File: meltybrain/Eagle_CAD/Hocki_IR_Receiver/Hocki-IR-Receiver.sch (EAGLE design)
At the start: 70 parts, among them J1 SM03B-SRSS-TB(LF)(SN), U1 OPA2380AIDGKR, U10 NL27WZ32USG, U11 TMUX1204DGSR, U2 OPA2380AIDGKR, U3 AP2210K-5.0TRG1, U4 LMH6612MAX/NOPB, U5 LMH6612MAX/NOPB, U6 TLV73310PDBVT, U7 TLV3502AIDCNR, U8 TLV3502AIDCNR, U9 SN74LVC1G58DCKR

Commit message: schematic updates
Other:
- moved on the sheet: C14, C16, R15, R26

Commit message: IR Receiver schematic edits. Added ldo protection
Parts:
- added D10, D11: BAS581-02V-V-G-08, Hocki_Library:BAS581-02V-V-G-08
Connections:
- net N$15 renamed 10KPEAK_BUF
- net N$16 renamed 1MPEAK_BUF
- net N$17 renamed 1MPEAK
- net N$18 renamed 100KPEAK_BUF
- net 1.0V: now also D11.A
- net 5V: now also D10.A, D11.C
- net 9V: now also D10.C
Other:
- note added: "Comparator W/ Hyst"
- note added: "Multiplexer And Connector"
- note added: "Multiplexer Logic: A1=A+B A0=A+!B!C"
- note added: "Peak Buffering"
- note added: "Peak Detector"
- note added: "Power Regulation"
- note added: "Transimpedance"
- note removed: "Logic: A1=A+B A0=A+!B!C"
- moved on the sheet: C1, C10, C11, C12, C13, C14, C15, C16, C17, C2, C3, C4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

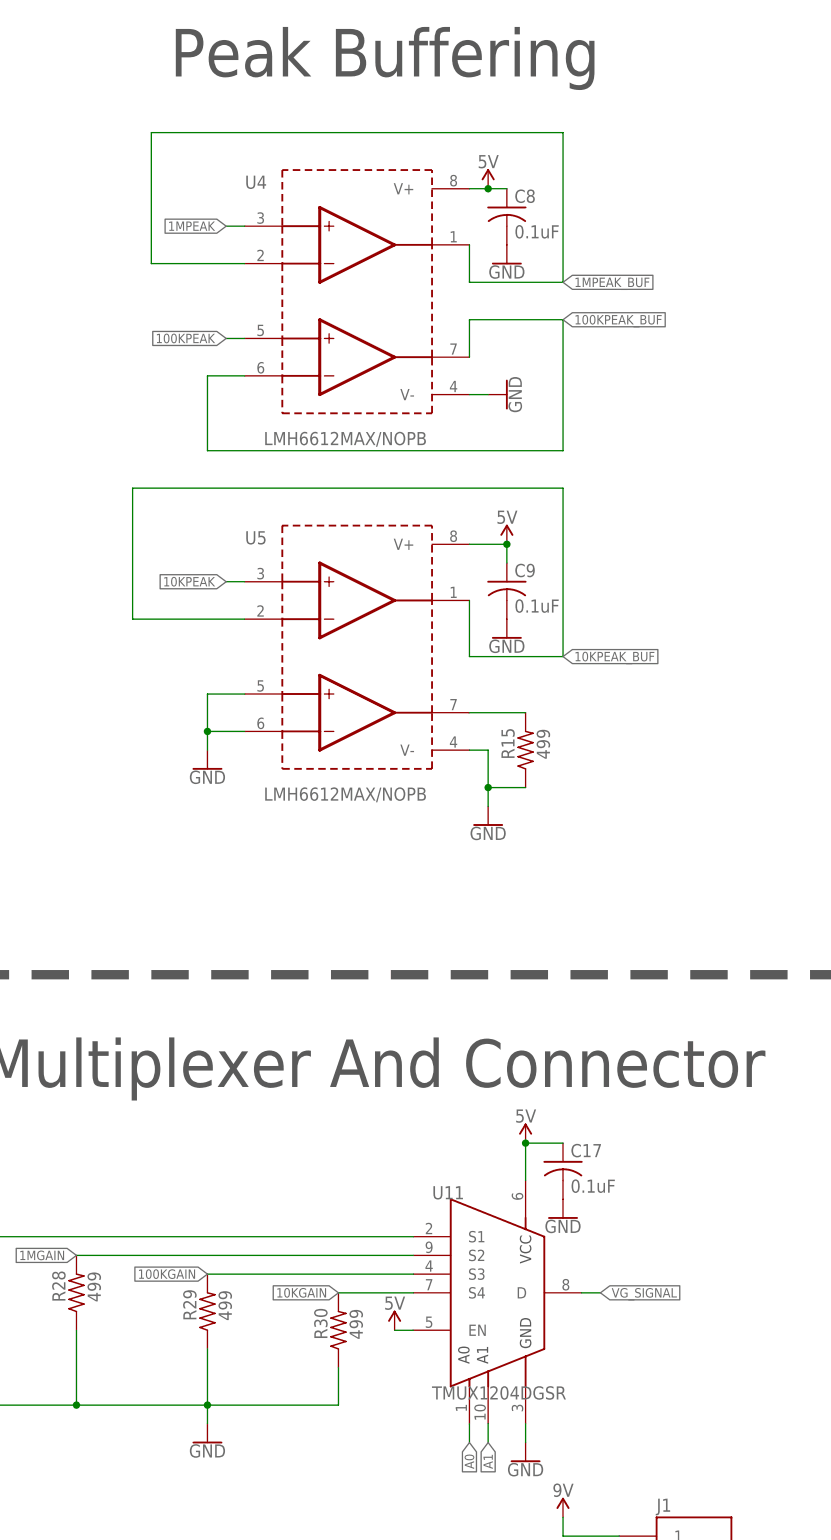
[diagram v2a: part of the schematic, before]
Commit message: Edited silkscreen and made minor changes to IR Receiver silkscreen and schematic
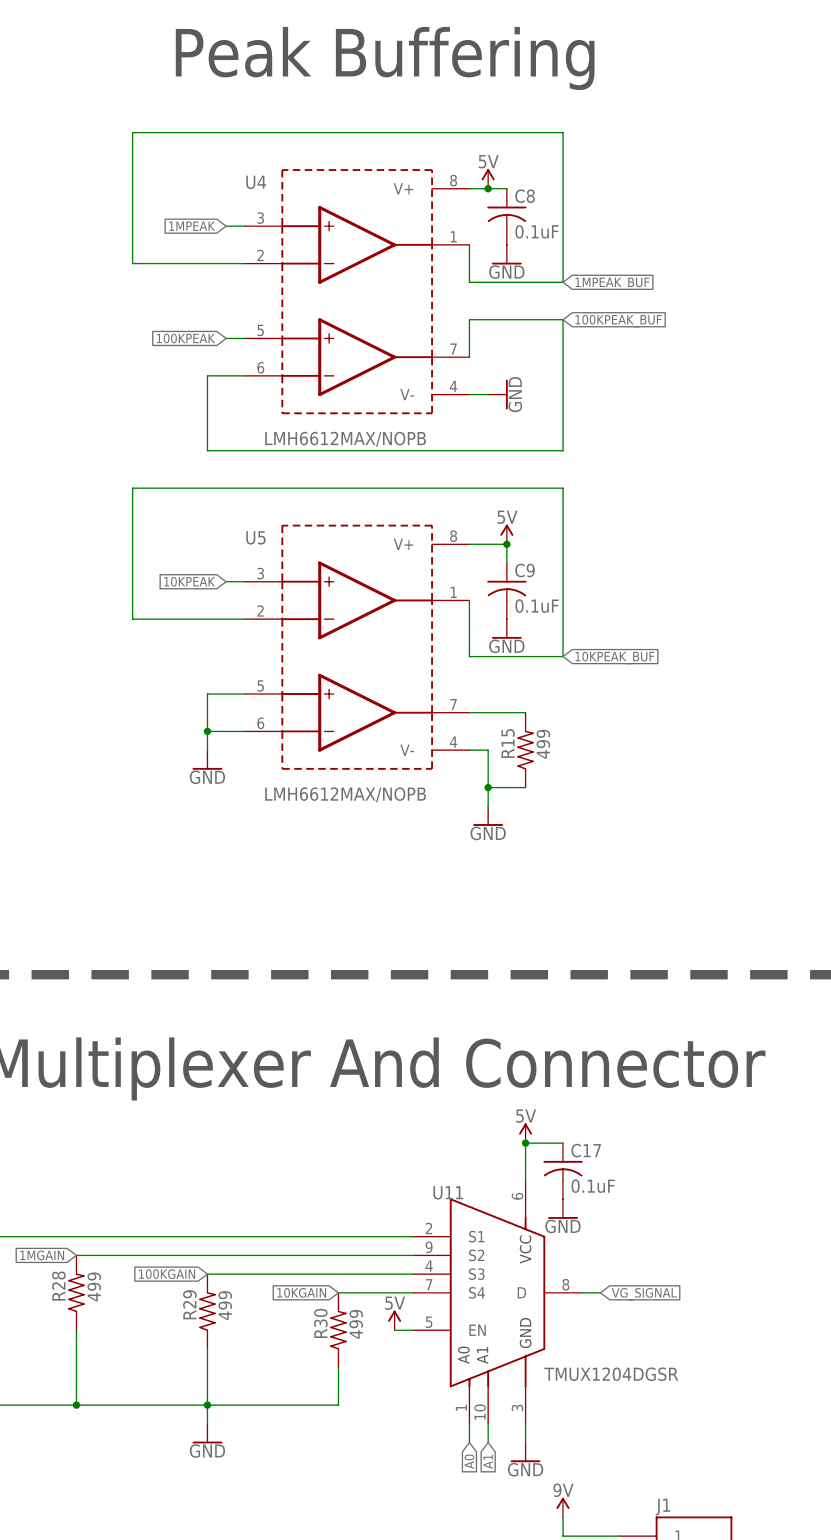
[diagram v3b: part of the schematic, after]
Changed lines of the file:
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@@
 <instance part="U11" gate="A" x="157.48" y="-43.18" smashed="yes">
 <attribute name="NAME" x="147.32" y="-30.48" size="1.778" layer="95"/>
-<attribute name="VALUE" x="147.32" y="-55.88" size="1.778" layer="96" align="top-left"/>
+<attribute name="VALUE" x="162.56" y="-53.34" size="1.778" layer="96" align="top-left"/>
 </instance>
 <instance part="R20" gate="G$1" x="-172.72" y="-25.4" smashed="yes" rot="R90">
@@
 <pinref part="U4" gate="A" pin="OUTA"/>
 <pinref part="U4" gate="A" pin="INA-"/>
-<wire x1="121.92" y1="96.52" x2="109.22" y2="96.52" width="0.1524" layer="91"/>
-<wire x1="109.22" y1="96.52" x2="109.22" y2="114.3" width="0.1524" layer="91"/>
-<wire x1="109.22" y1="114.3" x2="165.1" y2="114.3" width="0.1524" layer="91"/>
+<wire x1="121.92" y1="96.52" x2="106.68" y2="96.52" width="0.1524" layer="91"/>
+<wire x1="106.68" y1="96.52" x2="106.68" y2="114.3" width="0.1524" layer="91"/>
+<wire x1="106.68" y1="114.3" x2="165.1" y2="114.3" width="0.1524" layer="91"/>
 <wire x1="165.1" y1="93.98" x2="165.1" y2="114.3" width="0.1524" layer="91"/>
 <wire x1="152.4" y1="99.06" x2="152.4" y2="93.98" width="0.1524" layer="91"/>

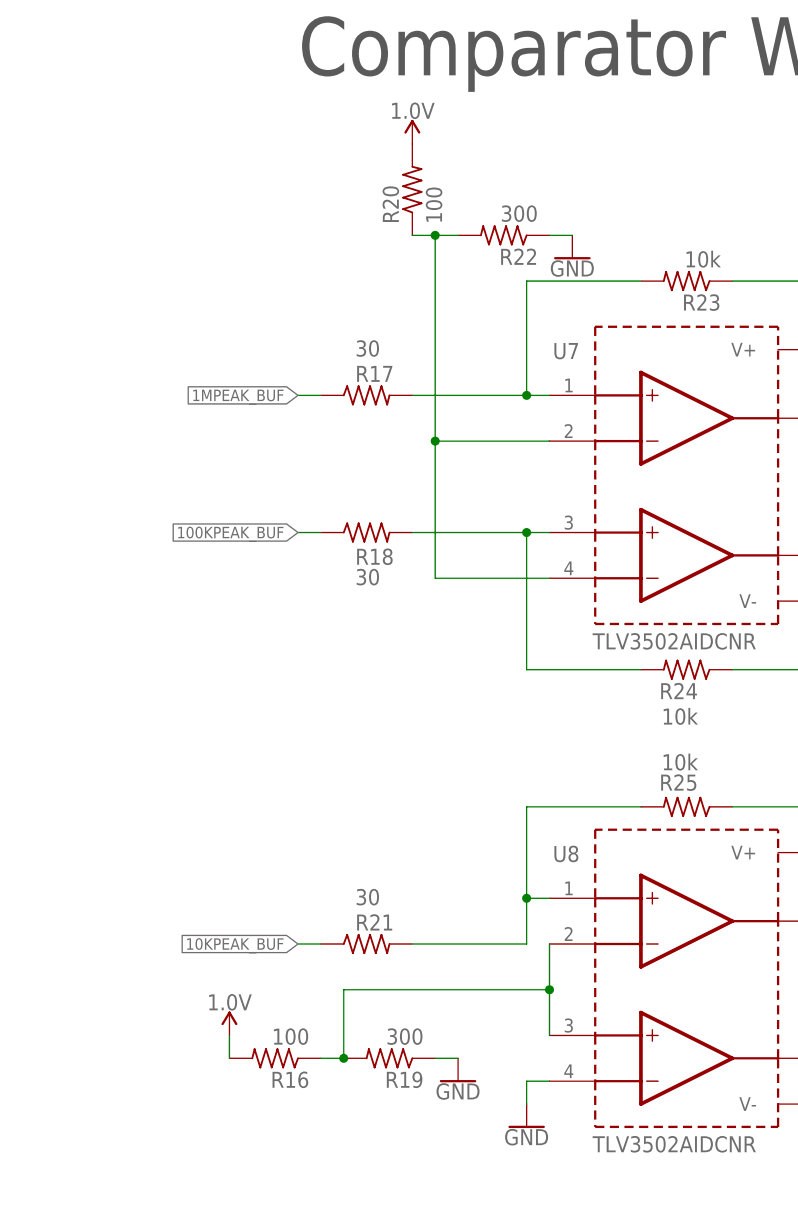
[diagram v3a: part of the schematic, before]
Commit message: comparator trigger point fixed
assumed diode voltage drop was constant originally
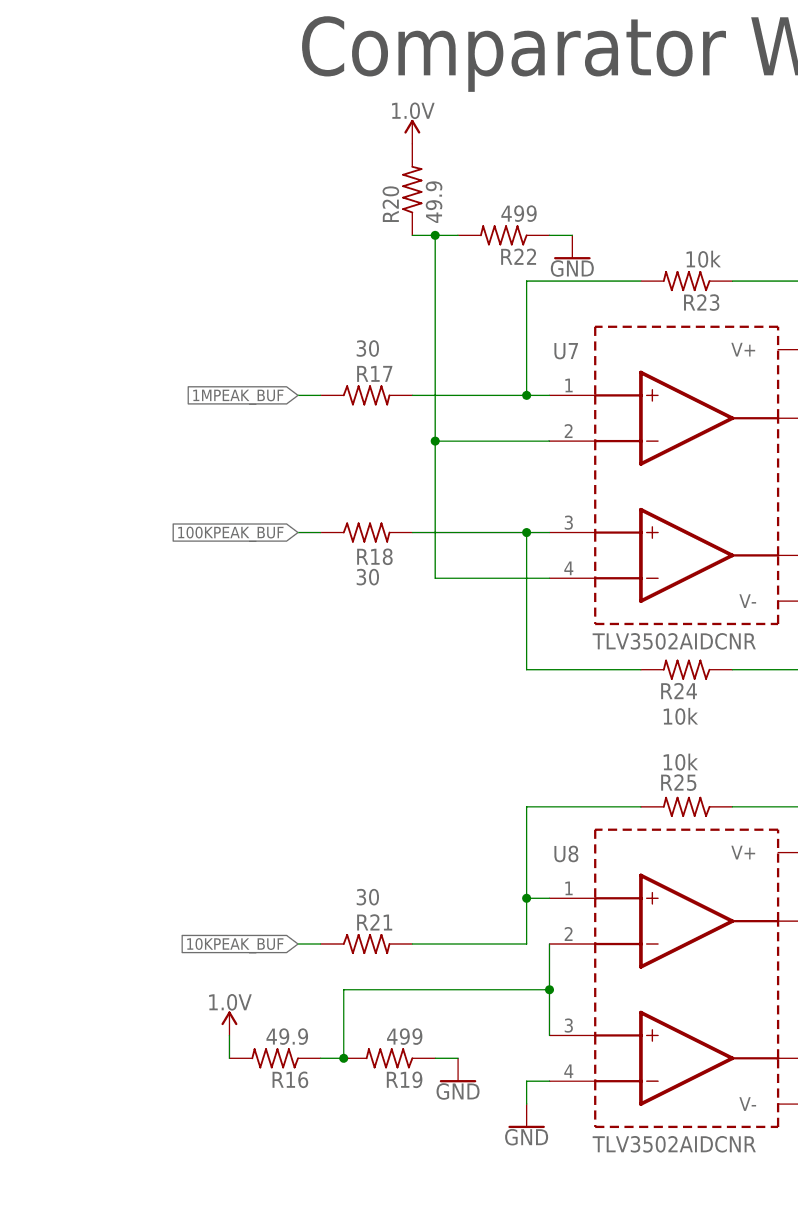
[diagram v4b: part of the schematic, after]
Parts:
- R16, R20: value 100 -> 49.9
- R19, R22: value 300 -> 499
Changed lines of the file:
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@@
 <part name="SUPPLY10" library="SparkFun-PowerSymbols" deviceset="5V" device=""/>
 <part name="U11" library="Hocki_Library" deviceset="TMUX1204DGSR" device=""/>
-<part name="R20" library="resistor" library_urn="urn:adsk.eagle:library:348" deviceset="R-US_" device="R0603" package3d_urn="urn:adsk.eagle:package:26057/1" value="100"/>
-<part name="R22" library="resistor" library_urn="urn:adsk.eagle:library:348" deviceset="R-US_" device="R0603" package3d_urn="urn:adsk.eagle:package:26057/1" value="300"/>
+<part name="R20" library="resistor" library_urn="urn:adsk.eagle:library:348" deviceset="R-US_" device="R0603" package3d_urn="urn:adsk.eagle:package:26057/1" value="49.9"/>
+<part name="R22" library="resistor" library_urn="urn:adsk.eagle:library:348" deviceset="R-US_" device="R0603" package3d_urn="urn:adsk.eagle:package:26057/1" value="499"/>
 <part name="GND14" library="SparkFun-PowerSymbols" deviceset="GND" device=""/>
-<part name="R16" library="resistor" library_urn="urn:adsk.eagle:library:348" deviceset="R-US_" device="R0603" package3d_urn="urn:adsk.eagle:package:26057/1" value="100"/>
-<part name="R19" library="resistor" library_urn="urn:adsk.eagle:library:348" deviceset="R-US_" device="R0603" package3d_urn="urn:adsk.eagle:package:26057/1" value="300"/>
+<part name="R16" library="resistor" library_urn="urn:adsk.eagle:library:348" deviceset="R-US_" device="R0603" package3d_urn="urn:adsk.eagle:package:26057/1" value="49.9"/>
+<part name="R19" library="resistor" library_urn="urn:adsk.eagle:library:348" deviceset="R-US_" device="R0603" package3d_urn="urn:adsk.eagle:package:26057/1" value="499"/>
 <part name="SUPPLY11" library="SparkFun-PowerSymbols" deviceset="5V" device=""/>
 <part name="GND15" library="SparkFun-PowerSymbols" deviceset="GND" device=""/>

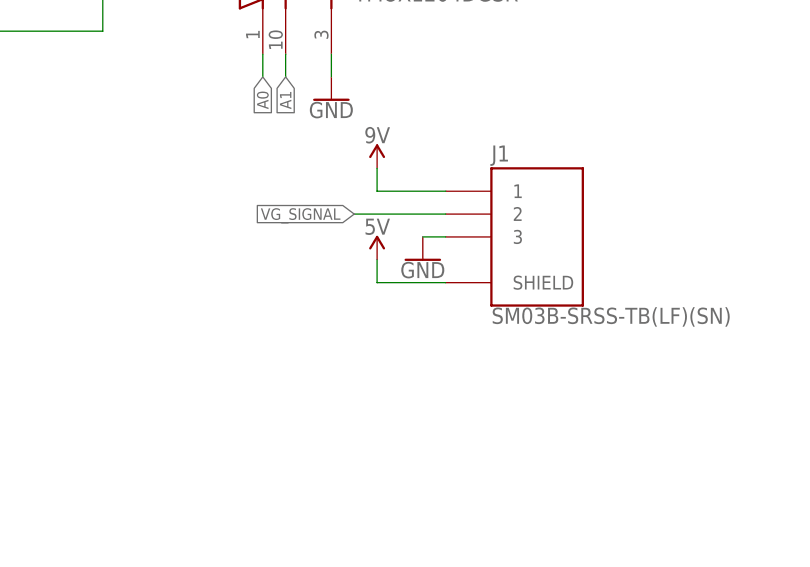
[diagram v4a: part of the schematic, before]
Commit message: receiver now 4 layers
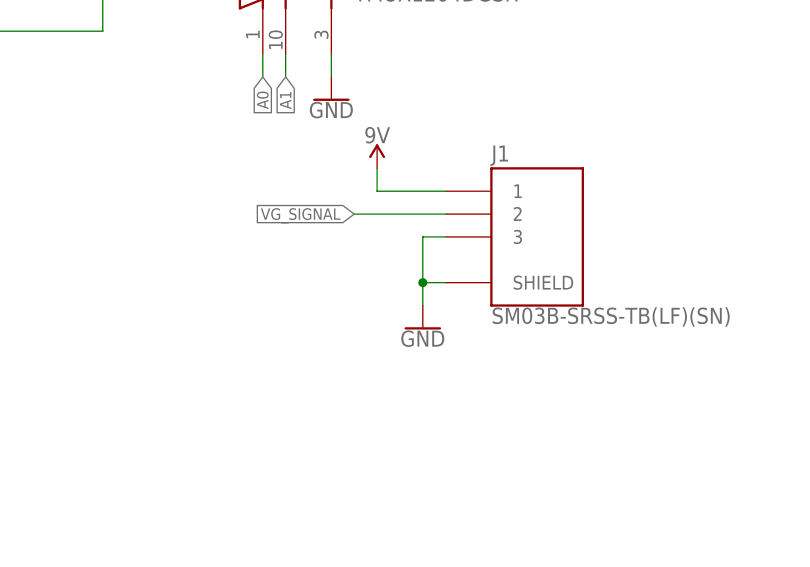
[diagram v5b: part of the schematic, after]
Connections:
- net 5V: no longer J1.SHIELD
- net GND: now also J1.SHIELD
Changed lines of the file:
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@@
 <part name="SUPPLY17" library="Hocki_Library" deviceset="9V" device=""/>
 <part name="GND34" library="SparkFun-PowerSymbols" deviceset="GND" device=""/>
-<part name="SUPPLY18" library="SparkFun-PowerSymbols" deviceset="5V" device=""/>
 <part name="J1" library="Hocki_Library" deviceset="SM03B-SRSS-TB(LF)(SN)" device="" package3d_urn="urn:adsk.eagle:package:22261818/2"/>
 <part name="D8" library="SparkFun-LED" deviceset="LED-GREEN" device="0603" value="GREEN"/>
@@
 <attribute name="VALUE" x="165.1" y="-70.866" size="1.778" layer="96" align="bottom-center"/>
 </instance>
-<instance part="GND34" gate="1" x="170.18" y="-83.82" smashed="yes">
-<attribute name="VALUE" x="170.18" y="-84.074" size="1.778" layer="96" align="top-center"/>
-</instance>
-<instance part="SUPPLY18" gate="G$1" x="165.1" y="-83.82" smashed="yes">
-<attribute name="VALUE" x="165.1" y="-81.026" size="1.778" layer="96" align="bottom-center"/>
+<instance part="GND34" gate="1" x="170.18" y="-91.44" smashed="yes">
+<attribute name="VALUE" x="170.18" y="-91.694" size="1.778" layer="96" align="top-center"/>
 </instance>
 <instance part="J1" gate="G$1" x="182.88" y="-81.28" smashed="yes">
@@
 <pinref part="J1" gate="G$1" pin="3"/>
 <wire x1="172.72" y1="-81.28" x2="170.18" y2="-81.28" width="0.1524" layer="91"/>
+<wire x1="170.18" y1="-81.28" x2="170.18" y2="-86.36" width="0.1524" layer="91"/>
+<pinref part="J1" gate="G$1" pin="SHIELD"/>
+<wire x1="170.18" y1="-86.36" x2="170.18" y2="-88.9" width="0.1524" layer="91"/>
+<wire x1="172.72" y1="-86.36" x2="170.18" y2="-86.36" width="0.1524" layer="91"/>
+<junction x="170.18" y="-86.36"/>
 </segment>
 <segment>
@@
 </segment>
 <segment>
-<wire x1="172.72" y1="-86.36" x2="165.1" y2="-86.36" width="0.1524" layer="91"/>
-<pinref part="SUPPLY18" gate="G$1" pin="5V"/>
-<wire x1="165.1" y1="-86.36" x2="165.1" y2="-83.82" width="0.1524" layer="91"/>
-<pinref part="J1" gate="G$1" pin="SHIELD"/>
-</segment>
-<segment>

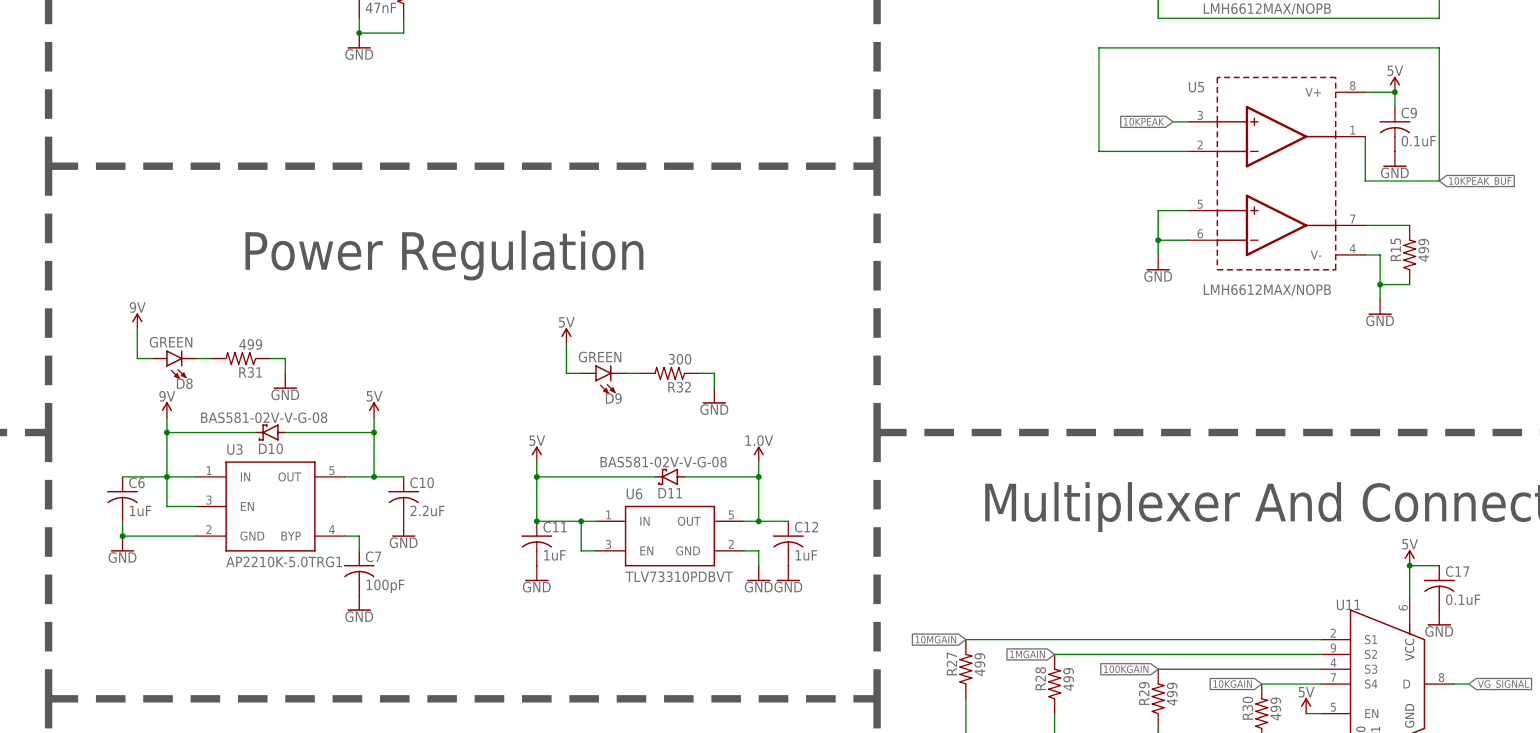
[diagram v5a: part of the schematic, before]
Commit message: tvs diodes and removed 1v regulator
1v supplied with free opamp
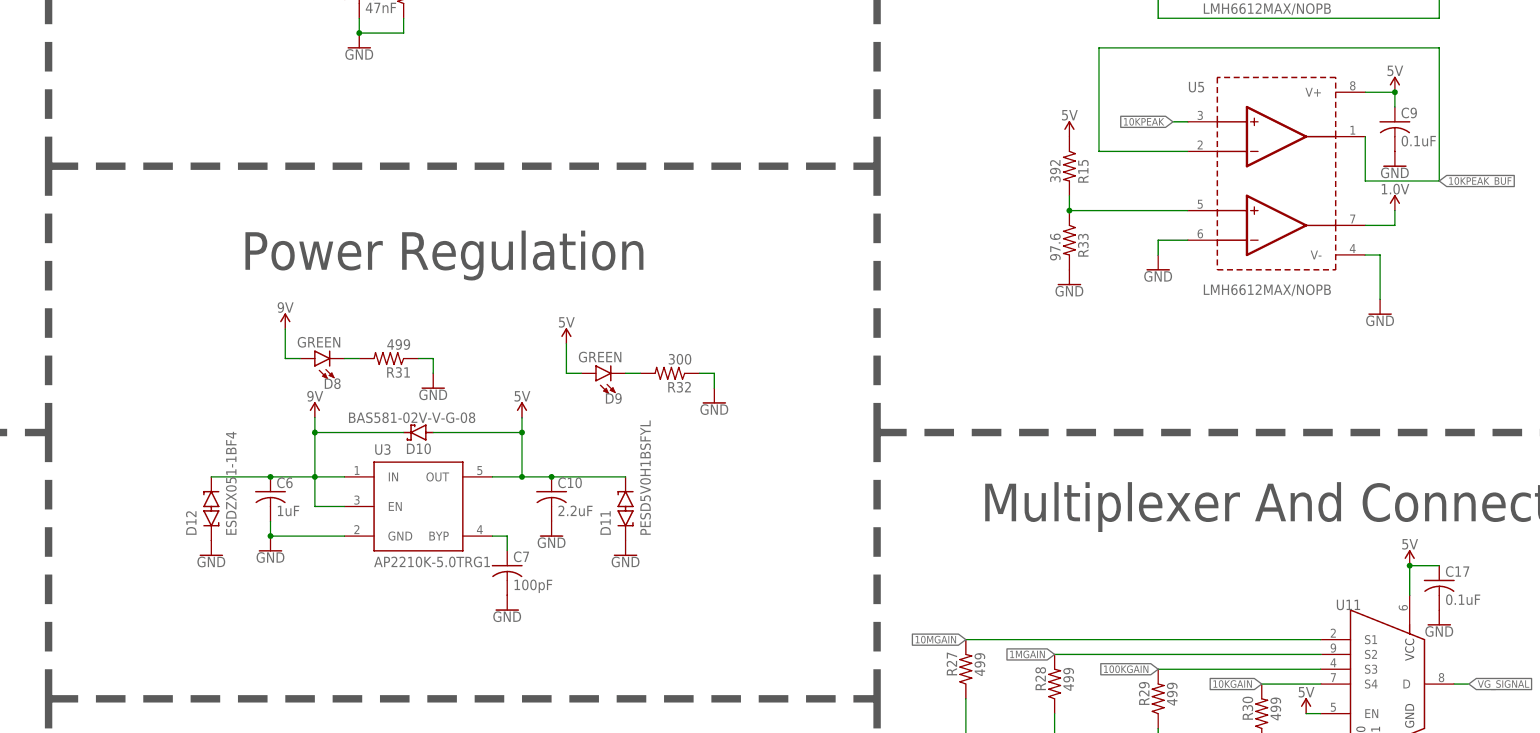
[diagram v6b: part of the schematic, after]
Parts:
- removed C11, C12: 1uF, rcl:C-USC0603
- removed U6: TLV73310PDBVT, Hocki_Library:TLV73310PDBVT
- added D12: ESDZX051-1BF4, Hocki_Library:ESDZX051-1BF4
- added R33: 97.6, resistor:R-US_R0603
- D11: value BAS581-02V-V-G-08 -> PESD5V0H1BSFYL; device Hocki_Library:BAS581-02V-V-G-08 -> Hocki_Library:PESD5V0H1BSFYL
- R15: value 499 -> 392
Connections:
- removed net N$19: R15.2, U5.OUTB
- new net N$15: R15.2, R33.1, U5.INB+
- net 1.0V: now also U5.OUTB; no longer C12.1, D11.A, U6.OUT
- net 5V: now also D11.C2, R15.1; no longer C11.1, D11.C, U6.EN, U6.IN
- net 9V: now also D12.C2
- net GND: now also D11.C1, D12.C1, R33.2; no longer C11.2, C12.2, R15.1, U5.INB+, U6.GND
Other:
- moved on the sheet: C10, C6, C7, D10, D8, R15, R31, U3
